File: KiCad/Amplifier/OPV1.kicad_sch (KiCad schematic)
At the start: 14 parts, among them U2 AD8021AR

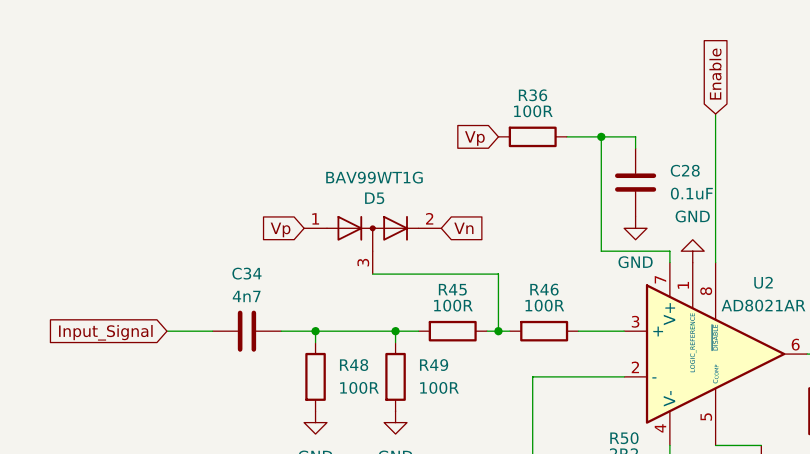
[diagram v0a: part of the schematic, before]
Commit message: Platinenentwurf
die Platine wurde aufgebaut. Kontrolle fehlt
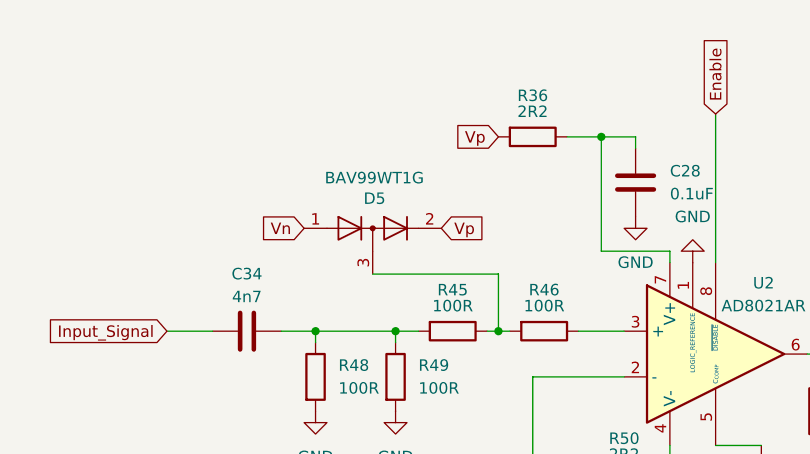
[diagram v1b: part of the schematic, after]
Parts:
- R36: value 100R -> 2R2
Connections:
- net Vn: now also D5.1 (K); no longer D5.2 (A)
- net Vp: now also D5.2 (A); no longer D5.1 (K)
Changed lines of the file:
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@@
 		)
 	)
-	(global_label "Vn"
+	(global_label "Vp"
 		(shape input)
 		(at 88.9 76.2 0)
@@
 		)
 	)
-	(global_label "Vp"
+	(global_label "Vn"
 		(shape input)
 		(at 73.66 76.2 180)
@@
 			)
 		)
-		(property "Value" "100R"
+		(property "Value" "2R2"
 			(at 99.06 63.246 90)
 			(effects
